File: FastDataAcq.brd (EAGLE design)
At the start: 114.3 x 62.7 mm, 215 parts, among them IC1 LT1963AEQ, IC2 FT230XQ, IC3 ADCMP553BRMZ, J1 MICRO-FIT_3.0_2POS_RA_SMD, J2 USB_MICROAB_SMT, X1 87832-14, X2 SMA-142-0701-801/806, X3 SMA-142-0701-801/806, Y1 SI530-500, Y2 100MHz, Y3 DNP

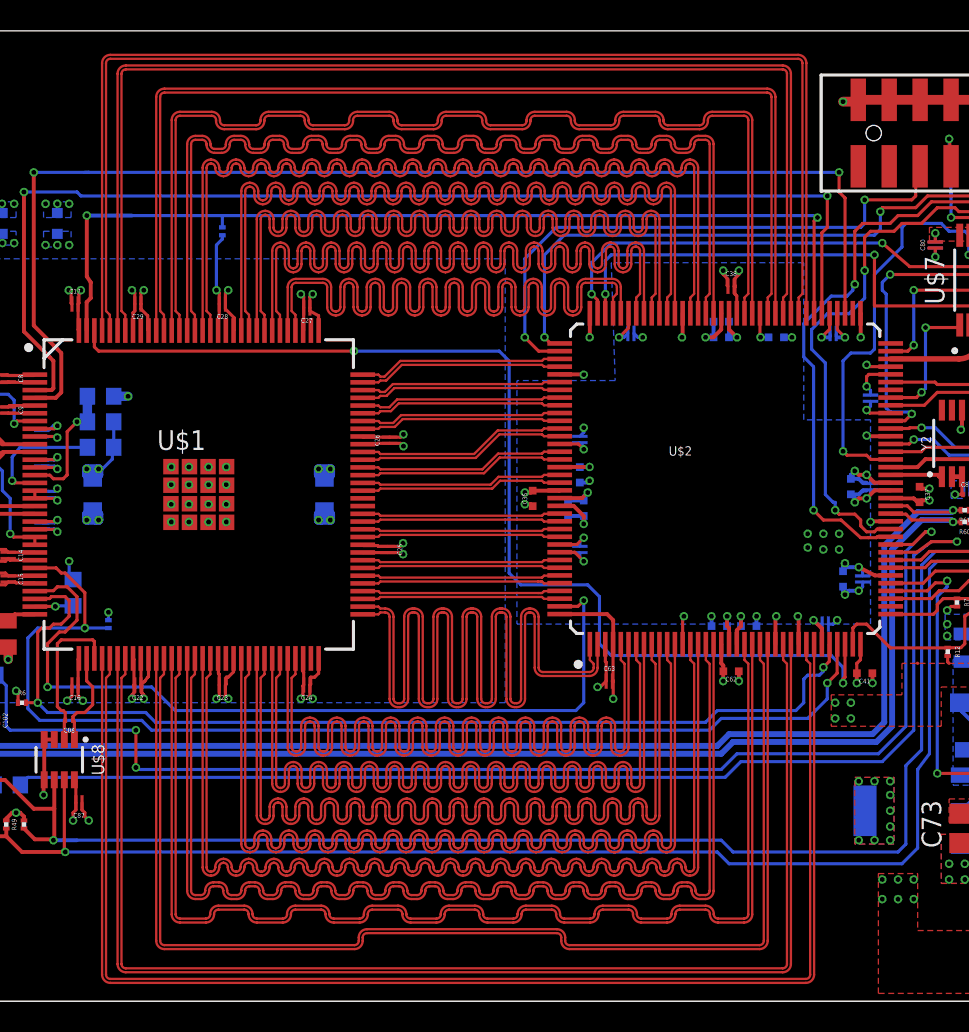
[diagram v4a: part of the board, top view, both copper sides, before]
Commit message: LVDS Top Changed
Changed LVDS data lines to 5mil width and spacing. Bend separation is
25mil.  Only the top data lines are finished - still need to do the
bottom and sides.
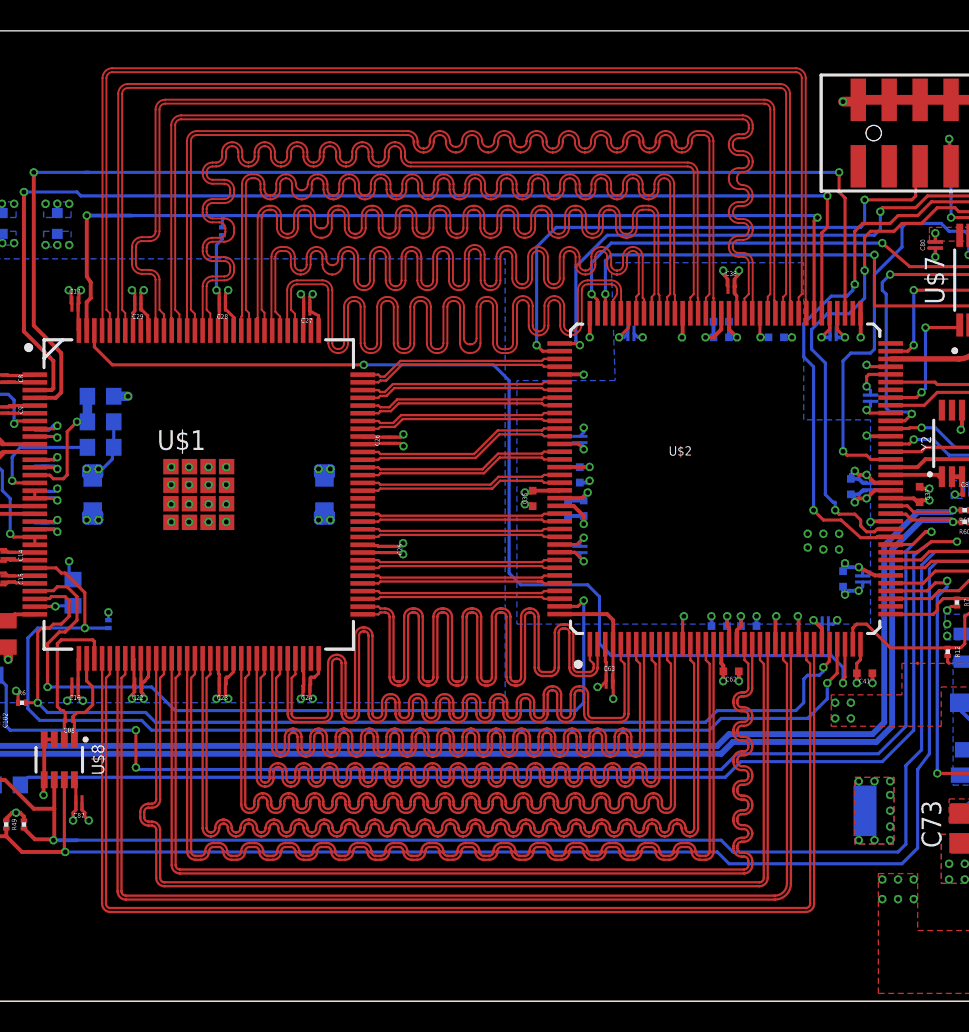
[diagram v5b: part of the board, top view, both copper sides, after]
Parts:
- C7, C75: value NA -> DNP
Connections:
- net DI0+ renamed DI0_P
- net DI0- renamed DI0_N
- net DI1+ renamed DI1_P
- net DI1- renamed DI1_N
- net DID0+ renamed DID0_P
- net DID0- renamed DID0_N
- net DID1+ renamed DID1_P
- net DID1- renamed DID1_N
- net DID2+ renamed DID2_P
- net DID2- renamed DID2_N
- net DID3+ renamed DID3_P
- net DID3- renamed DID3_N
- net DID4+ renamed DID4_P
- net DID4- renamed DID4_N
- net DID5+ renamed DID5_P
- net DID5- renamed DID5_N
- net DID6+ renamed DID6_P
- net DID6- renamed DID6_N
- net DID7+ renamed DID7_P
- net DID7- renamed DID7_N
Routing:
- net DQD1-: track 83.9 -> 74.2 mm
- net DQD1+: track 84.4 -> 74.7 mm
- net DI1_N: track 58.5 -> 67.9 mm
- net DQD0-: track 87.8 -> 78.6 mm
- net DQD0+: track 88.3 -> 79.1 mm
- net DQD6-: track 74.2 -> 65.0 mm
- net DQD6+: track 74.7 -> 65.6 mm
- net DQ2-: track 76.9 -> 68.1 mm
- net DQ2+: track 77.1 -> 68.3 mm
- net DI1_P: track 59.0 -> 67.8 mm
- net DQD7-: track 74.4 -> 65.8 mm
- net DQD7+: track 75.0 -> 66.3 mm
- net DQ0+: track 75.2 -> 67.1 mm
- net DQ0-: track 74.7 -> 66.6 mm
- net DQD2-: track 78.0 -> 69.9 mm
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
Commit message: Partially done with LVDS bottom half.
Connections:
- net DQ0+ renamed DQ0_P
- net DQ0- renamed DQ0_N
- net DQ1+ renamed DQ1_P
- net DQ1- renamed DQ1_N
- net DQ2+ renamed DQ2_P
- net DQ2- renamed DQ2_N
- net DQD0+ renamed DQD0_P
- net DQD0- renamed DQD0_N
- net DQD1+ renamed DQD1_P
- net DQD1- renamed DQD1_N
- net DQD2+ renamed DQD2_P
- net DQD2- renamed DQD2_N
- net DQD3+ renamed DQD3_P
- net DQD3- renamed DQD3_N
- net DQD4+ renamed DQD4_P
- net DQD4- renamed DQD4_N
- net DQD5+ renamed DQD5_P
- net DQD5- renamed DQD5_N
- net DQD6+ renamed DQD6_P
- net DQD6- renamed DQD6_N
- net DQD7+ renamed DQD7_P
- net DQD7- renamed DQD7_N
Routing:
- net DQD1_P: track 74.7 -> 81.4 mm
- net DQD1_N: track 74.2 -> 80.8 mm
- net DQD0_P: track 79.1 -> 85.7 mm
- net DQD0_N: track 78.6 -> 85.1 mm
- net DQD6_P: track 65.6 -> 71.6 mm
- net DQD7_N: track 65.8 -> 71.8 mm
- net DQD6_N: track 65.0 -> 71.0 mm
- net DQD7_P: track 66.3 -> 72.2 mm
- net DQ1_N: track 67.1 -> 72.4 mm
- net DQD2_P: track 70.4 -> 75.6 mm
- net DQ2_N: track 68.1 -> 73.2 mm
- net DQ0_N: track 66.6 -> 71.6 mm
- net DQD2_N: track 69.9 -> 74.9 mm
- net DQ2_P: track 68.3 -> 73.2 mm
- net DQ1_P: track 67.6 -> 72.4 mm
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
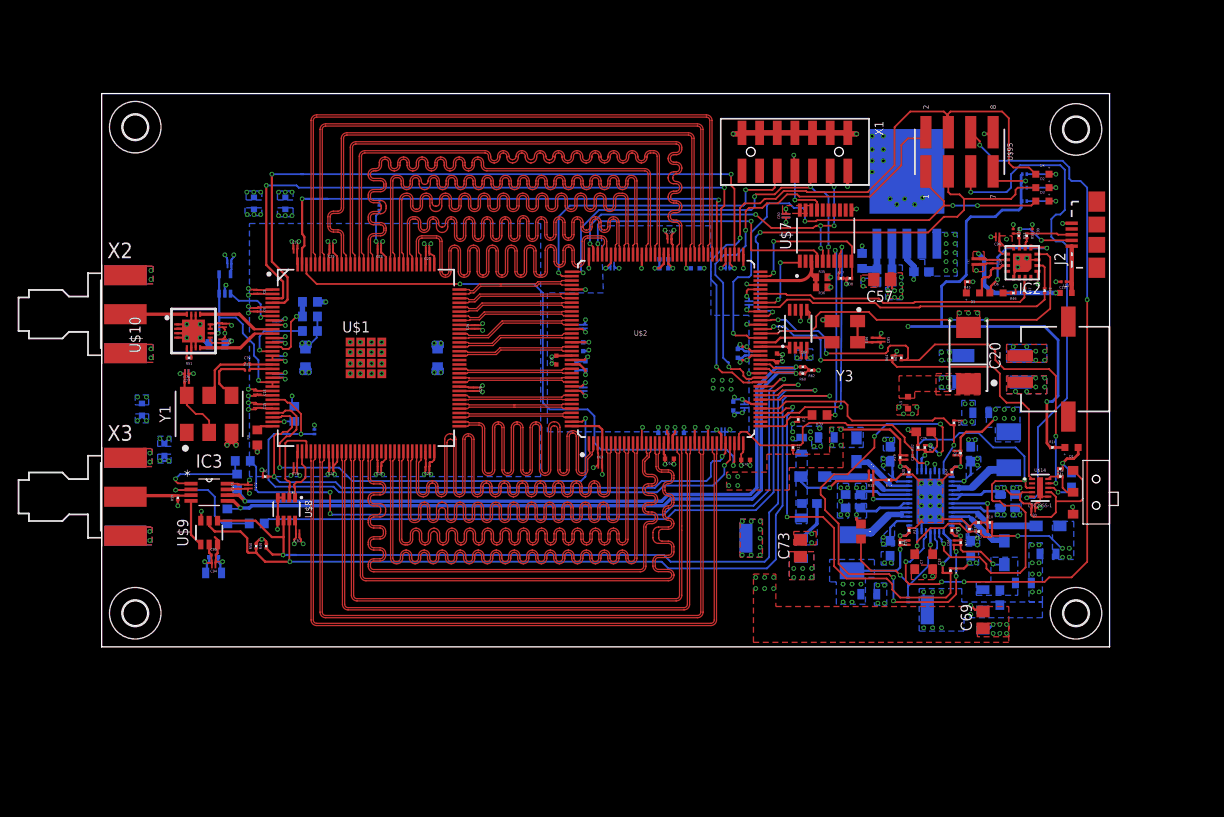
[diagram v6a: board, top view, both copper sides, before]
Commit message: Finished LVDS layout.
Making additional final changes. Still need to add test points.
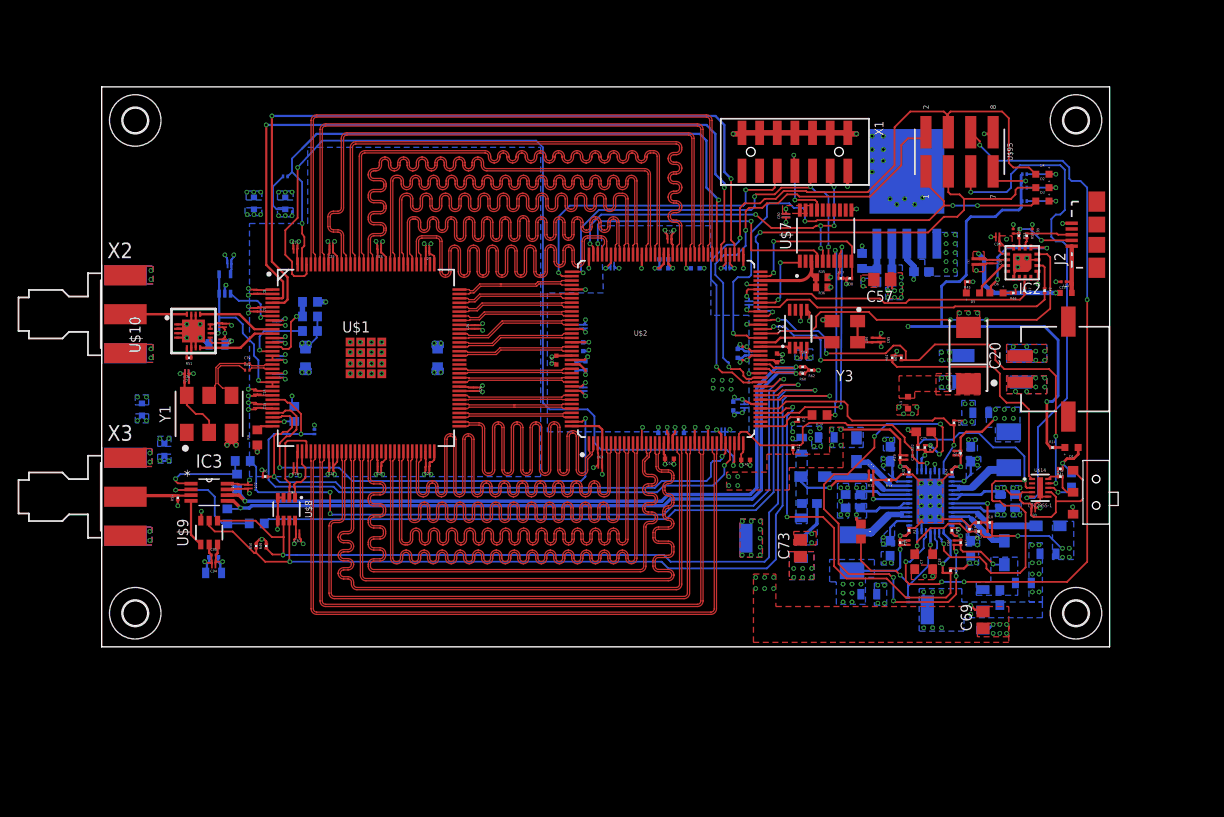
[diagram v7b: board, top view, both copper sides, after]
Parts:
- moved R1 11.2 mm to (20.8, 70.6), turned to 0 degrees
- moved H2 1.02 mm to (110.5, 77.0)
- moved H4 0.76 mm to (3.81, 77.0)
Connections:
- net ADC_CLK+ renamed ADC_CLK_P
- net ADC_CLK- renamed ADC_CLK_N
- net CLK500+ renamed CLK500_P
- net CLK500- renamed CLK500_N
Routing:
- net ADC_CALRUN: track 70.7 -> 103.8 mm
- net ADC_CALDLY/DES/!SCS: track 62.3 -> 75.6 mm
- net ADC_OUTV/SCLK: track 74.5 -> 87.2 mm
- net ADC_OUTEDGE/DDR/SDATA: track 78.4 -> 90.3 mm
- net DQD3_P: track 71.7 -> 74.6 mm
- net DQD3_N: track 71.0 -> 73.9 mm
- net DQD0_P: track 85.7 -> 83.1 mm
- net DQD1_P: track 81.4 -> 78.8 mm
- net DQD1_N: track 80.8 -> 78.2 mm
- net DQD0_N: track 85.1 -> 82.6 mm
- net 1V9D: track 29.2 -> 31.3 mm
- net GND: track 234.0 -> 233.0 mm
- net FPGA_SCL: track 105.2 -> 104.3 mm
- net DQD4_P: track 73.4 -> 74.2 mm
- net PWR_KILL: track 55.4 -> 54.6 mm
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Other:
- board size 114.3 x 62.7 mm -> 114.3 x 63.5 mm
- board text added: "Manufacturer Notes: 1. All copper thickness is 1oz 2. LVDS lines are 5mil width with 5mil spacing and should have a 100 Ohms+/- 10% differential impedance. 3. Layer height is betwen 7 and 8 mils."

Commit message: Parts finalized. Layout near done.
Still a few things on the to do list, but most tracks are final. Still
need test points and to go over all text that's getting printed.
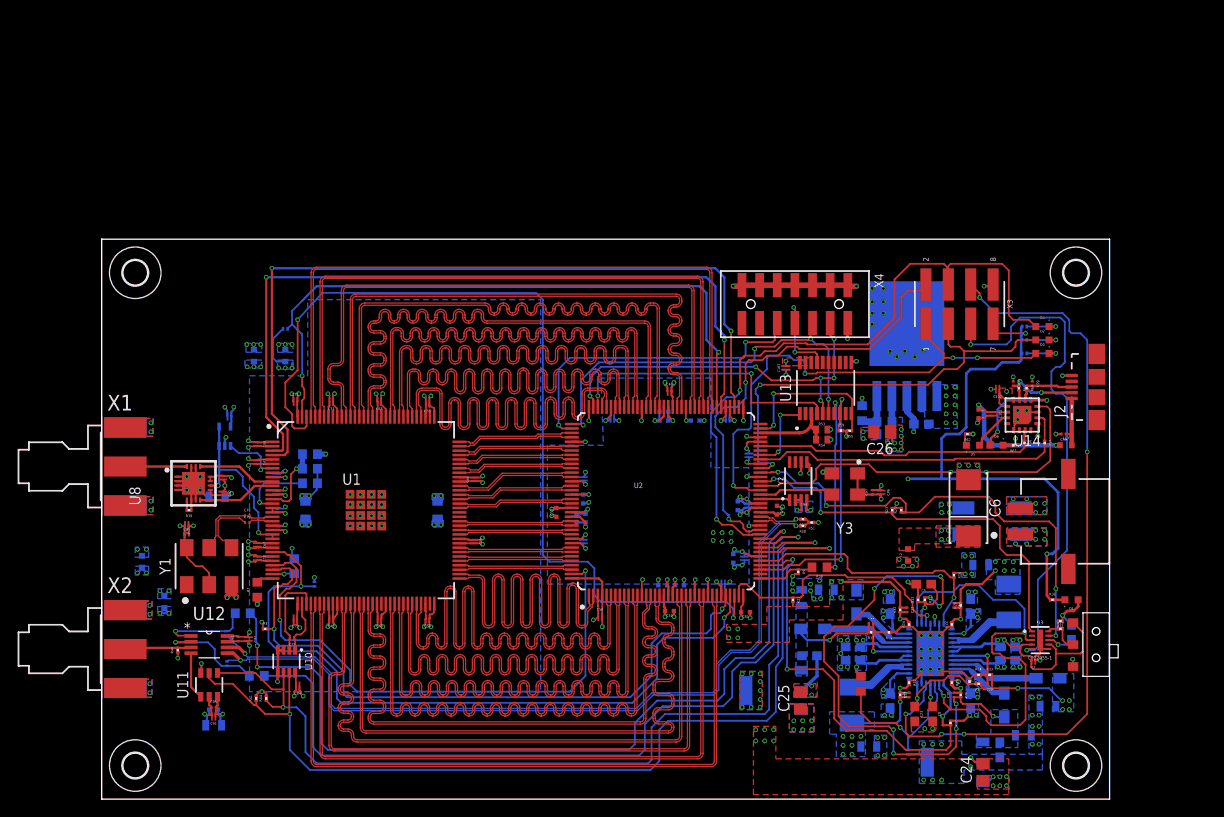
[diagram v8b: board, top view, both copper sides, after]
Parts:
- removed IC1: LT1963AEQ, linear-technology:Q5-DD
- removed IC2: FT230XQ, ftdichip:QFN16
- removed IC3: ADCMP553BRMZ, Schuyler:SOP65P490X110-8N
- removed R64: 523K, rcl:R0201
- removed U$1: ADC08D500, Schuyler:128HLQFP
- removed U$10: LMH6555, Schuyler:16WQFN
- removed U$11: LMV321SC-70, Schuyler:SC-70
- removed U$14: LTC2955-1, Schuyler:10-DFN
- removed U$2: XC6SLX9-3TQG144C, Schuyler:TQG144
- removed U$4: LTC3374QFN, Schuyler:38-QFN_(5X7)
- removed U$5: LT1963AEST-2.5, Schuyler:SOT223
- removed U$6: LT1963AEST-3.3, Schuyler:SOT223
- removed U$7: XCFXXS04, Schuyler:TSSOP20_XILINX
- removed U$8: TMP421, Schuyler:SOT23-8
- removed U$9: DAC101C081, Schuyler:SOT23-6
- removed U$95: HEADER_0.1"_8P_2R_SMT, Schuyler:HEADER_8P_2R_SMT
- added R58: 0, rcl:R0603
- added U1: ADC08D500, Schuyler:128HLQFP
- added U10: TMP421, Schuyler:SOT23-8
- added U11: DAC101C081, Schuyler:SOT23-6
- added U12: ADCMP553BRMZ, Schuyler:SOP65P490X110-8N
- added U13: XCFXXS04, Schuyler:TSSOP20_XILINX
- added U14: FT230XQ, ftdichip:QFN16
- added U2: XC6SLX9-3TQG144C, Schuyler:TQG144
- added U3: LTC2955-1, Schuyler:10-DFN
- added U4: LT1963AEST-2.5, Schuyler:SOT223
- added U5: LT1963AEST-3.3, Schuyler:SOT223
- added U6: LT1963AEQ, linear-technology:Q5-DD
- added U7: LTC3374QFN, Schuyler:38-QFN_(5X7)
- added U8: LMH6555, Schuyler:16WQFN
- added U9: LMV321SC-70, Schuyler:SC-70
- added X4: 87832-14, con-molex:87832-14
- C10, C11, C14, C27, C28, C29: value .1uF -> 10pF; device Schuyler:0204REVERSE -> rcl:C0201
- C101, C103, C84, C86: value 10nF -> .1uF; device rcl:C0201 -> Schuyler:0204REVERSE
- C102, C81: value 1uF -> .1uF
- C104, C87, C90: value .1uF -> 1uF
- C105: value DNP -> 4.7uF; device rcl:C0603 -> Schuyler:0402_C
- C12, C13, C15, C30, C83: value .1uF -> 33uF; device Schuyler:0204REVERSE -> SparkFun-Passives:0805
- C16, C17, C22, C8: value .1uF -> 10uF; device Schuyler:0204REVERSE -> rcl:C0603
- C19, C3: value 33uF -> 10uF; device SparkFun-Passives:0805 -> rcl:C0603
- C2: value 10pF -> 10uF; device rcl:C0201 -> rcl:C0603
- C20: value 100uF -> 10uF; device Schuyler:2917_MURATA_CAP -> rcl:C0603
- C23, C9: value .1uF -> DNP; device Schuyler:0204REVERSE -> rcl:C0603
- C24, C25, C26: value .1uF -> 22uF 150mOhm ESR; device Schuyler:0204REVERSE -> rcl:C0805
- C32: value 10uF -> 33uF; device rcl:C0603 -> SparkFun-Passives:0805
- C33, C66: value 10pF -> 4.7uF; device rcl:C0201 -> Schuyler:0402_C
- C34, C74: value 33uF -> 4.7uF; device SparkFun-Passives:0805 -> Schuyler:0402_C
- C37, C42, C43, C62: value 4.7uF -> 0.47uF; device Schuyler:0402_C -> Schuyler:0204REVERSE
- C39, C40: value 4.7uF -> 33uF; device Schuyler:0402_C -> SparkFun-Passives:0805
- C44, C45, C47, C50, C59: value 4.7uF -> .1uF; device Schuyler:0402_C -> Schuyler:0204REVERSE
- C48, C49, C60, C64: value 0.47uF -> .1uF
- C5: value 10pF -> DNP; device rcl:C0201 -> rcl:C0603
- C51, C52, C61: value 0.47uF -> 4.7uF; device Schuyler:0204REVERSE -> Schuyler:0402_C
- C53, C72: value 10uF -> 4.7uF; device rcl:C0603 -> Schuyler:0402_C
- C54, C71: value 10pF -> .1uF; device rcl:C0201 -> Schuyler:0204REVERSE
- C55, C67, C91: value 33uF -> .1uF; device SparkFun-Passives:0805 -> Schuyler:0204REVERSE
- C56, C58: value 10uF -> 0.47uF; device rcl:C0603 -> Schuyler:0204REVERSE
- C57, C69: value 22uF 150mOhm ESR -> 4.7uF; device rcl:C0805 -> Schuyler:0402_C
- C6: value 33uF -> 100uF; device SparkFun-Passives:0805 -> Schuyler:2917_MURATA_CAP
- C65, C68, C70: value 10uF -> .1uF; device rcl:C0603 -> Schuyler:0204REVERSE
- C7, C75: value DNP -> .1uF; device rcl:C0603 -> Schuyler:0204REVERSE
- C73: value 22uF 150mOhm ESR -> .1uF; device rcl:C0805 -> Schuyler:0204REVERSE
- C76: value 10nF -> 0.47uF; device rcl:C0201 -> Schuyler:0204REVERSE
- C77: value .1uF -> 100pF; device Schuyler:0204REVERSE -> rcl:C0201
- C78: value 1uF -> 4.7nF; device Schuyler:0204REVERSE -> rcl:C0201
- C82: value 4.7nF -> .1uF; device rcl:C0201 -> Schuyler:0204REVERSE
- C85, C94, C97: value .1uF -> 10nF; device Schuyler:0204REVERSE -> rcl:C0201
- C88: value 100pF -> 33uF; device rcl:C0201 -> SparkFun-Passives:0805
- C89: value .1uF -> 4.7uF; device Schuyler:0204REVERSE -> Schuyler:0402_C
- C92: value 4.7uF -> .1uF; device Schuyler:0306REVERSE -> Schuyler:0204REVERSE
- C93: value 4.7uF -> 10nF; device Schuyler:0402_C -> rcl:C0201
- C98: value 33uF -> 10nF; device SparkFun-Passives:0805 -> rcl:C0201
- L1: value 2.2uH -> CHOKE_CM_ACM7060-301; device Schuyler:3.0X3.6_VISHAY -> Schuyler:ACM7060_CHOKE
- L10, L9: value 2.2uH -> 26; device Schuyler:3.0X3.6_VISHAY -> Schuyler:MURATA_BLM18
- L2: value CHOKE_CM_ACM7060-301 -> 26; device Schuyler:ACM7060_CHOKE -> Schuyler:MURATA_BLM18
- L3: device Schuyler:5.18X5.49_VISHAY -> Schuyler:3.0X3.6_VISHAY
- L4, L6: value 26 -> 2.2uH; device Schuyler:MURATA_BLM18 -> Schuyler:3.0X3.6_VISHAY
- L5: value 26 -> 2.2uH; device Schuyler:MURATA_BLM18 -> Schuyler:5.18X5.49_VISHAY
- R1, R6: value 10k -> DNP; device rcl:R0201 -> rcl:R0603
- R10, R16: value 210K -> 523K
- R11: value 422K -> 649K
- R12: value 10k -> 150K
- R13, R17: value 270k -> 523K
- R14: value 330 -> 523K
- R15: value 845k -> 113k
- R18, R28: value 523K -> 210K
- R19: value 806K -> 150K
- R20: value 649K -> 523K
- R21: value 523K -> 10k
- R22: value 1.15k 1% -> 280K; device rcl:R0603 -> rcl:R0201
- R24: value 280K -> 523K
- R25: value 100 -> 523K; device rcl:R0603 -> rcl:R0201
- R26: value 2k 1% -> DNP
- R27: value 523K -> 270k
- R29: value 210K -> 1.15k 1%; device rcl:R0201 -> rcl:R0603
- R3, R8: value DNP -> 10k; device rcl:R0603 -> rcl:R0201
- R30: value 649K -> 2k 1%; device rcl:R0201 -> rcl:R0603
- R31: value 523K -> 100; device rcl:R0201 -> rcl:R0603
- R32: value 150K -> 806K
- R33: value 150K -> 210K
- R34: value 523K -> 649K
- R35: value 100 0.1% -> 845k; device rcl:R0402 -> rcl:R0201
- R36: value 100 0.1% -> 422K; device rcl:R0402 -> rcl:R0201
- R37: value 4.7k -> 270k
- R39: value 0 -> 50; device rcl:R0603 -> rcl:R0201
- R40: value DNP -> 50; device rcl:R0603 -> rcl:R0201
- R41: value 113k -> 10k
- R42: value 330 -> 26.1k; device rcl:R0201 -> rcl:R0603
- R43, R44, R47: value 330 -> 10k
- R46: value 330 -> 16k; device rcl:R0201 -> rcl:R0603
- R49: value 10k -> 330
- R50: value 10k -> 50
- R52: value 27 -> 50
- R53: value 27 -> 100 0.1%; device rcl:R0201 -> rcl:R0402
- R54: value 26.1k -> 100 0.1%; device rcl:R0603 -> rcl:R0402
- R55: value 16k -> 330; device rcl:R0603 -> rcl:R0201
- R56, R57: value 10k -> 330; device rcl:R0603 -> rcl:R0201
- R59: value 50 -> 4.7k
- R60, R61: value 50 -> 27
- R62: value 50 -> 330
- R63: value 523K -> 330
- R7: value 4.7k -> 3.3k 0.1%; device rcl:R0201 -> rcl:R0603
- R9: value 3.3k 0.1% -> 4.7k; device rcl:R0603 -> rcl:R0201
- X1: value 87832-14 -> SMA-142-0701-801/806; device con-molex:87832-14 -> con-coax:J502-ND-142-0701-801/806
- X3: value SMA-142-0701-801/806 -> HEADER_0.1"_8P_2R_SMT; device con-coax:J502-ND-142-0701-801/806 -> Schuyler:HEADER_8P_2R_SMT
- moved R44 104.5 mm to (18.7, 11.4), flipped to the top, turned to 90 degrees
- moved R43 103.0 mm to (14.1, 18.8), turned to 270 degrees
- moved R42 100.9 mm to (16.0, 21.1), turned to 0 degrees
- moved R47 99.8 mm to (14.2, 15.4), flipped to the bottom, turned to 90 degrees
- moved X3 99.7 mm to (97.3, 56.1)
- moved C9 99.3 mm to (110.0, 18.9), flipped to the bottom
- moved C98 97.7 mm to (109.1, 41.4), flipped to the top
- moved R46 96.1 mm to (17.6, 14.0), flipped to the bottom, turned to 0 degrees
- moved C12 94.9 mm to (104.5, 7.24), turned to 180 degrees
- moved R41 94.8 mm to (17.5, 11.4), turned to 90 degrees
- moved R57 91.7 mm to (106.9, 40.4), flipped to the top
- moved R56 90.8 mm to (104.6, 40.4), flipped to the top, turned to 270 degrees
- moved C8 90.3 mm to (94.2, 9.65), turned to 270 degrees
- moved R49 89.5 mm to (104.6, 53.6), flipped to the bottom, turned to 180 degrees
- moved L9 88.0 mm to (17.3, 50.3), turned to 90 degrees
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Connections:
- removed net FPGA_TRIG+: IC3.6, R57.2, R61.2, U$2.P$51
- removed net FPGA_TRIG-: IC3.5, R56.2, R60.2, U$2.P$50
- new net FPGA_TRIG_N: R47.2, R50.2, U12.5, U2.P$50
- new net FPGA_TRIG_P: R43.2, R52.2, U12.6, U2.P$51
- net !PB: now also U3.P$5, X3.P$5; no longer U$14.P$5, U$95.P$5
- net !RXLED: now also U14.11; no longer IC2.11
- net !TXLED: now also U14.5; no longer IC2.5
- net 1V2: now also C28.1, C31.1, C33.P$1, C41.P$1, C46.P$1, L7.P$2, R27.1, R33.2, U2.P$128, U2.P$19, U2.P$28, U2.P$52, U2.P$89; no longer C2.1, C3.1, C35.P$1, C37.P$1, C38.P$1, L1.P$2, R10.2, R13.1, U$2.P$128, U$2.P$19, U$2.P$28, U$2.P$52, U$2.P$89
- net 1V8: now also C27.1, C30.1, C34.P$1, C38.P$1, C42.P$1, C56.P$1, C58.P$1, L6.P$2, R21.2, R32.2, U2.P$103, U2.P$122, U2.P$125, U2.P$135, U2.P$144, U2.P$18, U2.P$31, U2.P$4, U2.P$76, U2.P$86; no longer C33.1, C34.1, C47.P$1, C48.P$1, C49.P$1, C50.P$1, C64.P$1, L7.P$2, R12.2, R19.2, U$2.P$103, U$2.P$122, U$2.P$125, U$2.P$135, U$2.P$144, U$2.P$18, U$2.P$31, U$2.P$4, U$2.P$76, U$2.P$86
- net 1V9: now also C26.1, L10.P$1, L9.P$1, R29.2, R31.2, U6.4; no longer C57.1, IC1.4, L4.P$1, L6.P$1, R22.2, R25.2
- net 1V9A: now also C39.1, C44.P$1, C47.P$2, C49.P$2, C54.P$1, C59.P$1, C64.P$2, C67.P$1, C70.P$1, C73.P$2, C75.P$1, L9.P$2, R3.1, R6.2, U1.P$128, U1.P$13, U1.P$16, U1.P$17, U1.P$2, U1.P$20, U1.P$25, U1.P$28, U1.P$33, U1.P$5, U1.P$8; no longer C10.P$2, C11.P$1, C12.P$1, C13.P$2, C14.P$1, C15.P$1, C16.P$2, C17.P$1, C19.1, C8.P$1, C9.P$2, L4.P$2, R6.1, R8.2, U$1.P$128, U$1.P$13, U$1.P$16, U$1.P$17, U$1.P$2, U$1.P$20, U$1.P$25, U$1.P$28, U$1.P$33, U$1.P$5, U$1.P$8
- net 1V9D: now also C40.1, C45.P$1, C48.P$1, C50.P$1, C55.P$1, C60.P$1, C65.P$1, C68.P$1, C71.P$1, L10.P$2, R8.2, U1.P$110, U1.P$121, U1.P$40, U1.P$51, U1.P$62, U1.P$73, U1.P$88, U1.P$99; no longer C22.P$1, C23.P$1, C24.P$1, C25.P$1, C26.P$1, C27.P$1, C28.P$1, C29.P$1, C31.1, L6.P$2, R2.2, U$1.P$110, U$1.P$121, U$1.P$40, U$1.P$51, U$1.P$62, U$1.P$73, U$1.P$88, U$1.P$99
- net 2V3_1V9PRE: now also C14.1, C15.1, C19.1, L5.P$2, R20.2, U6.1, U6.2; no longer C54.1, C55.1, C56.1, IC1.1, IC1.2, L8.P$2, R21.2
- net 2V5: now also C24.1, L12.P$2, U4.3; no longer C69.1, L11.P$2, U$5.3
- net 2V5A: now also C85.1, C86.P$1, C87.P$1, L12.P$1; no longer C76.1, C77.P$1, C78.P$1, L11.P$1
- net 2V8_2V5PRE: now also C10.1, C12.1, C16.1, L3.P$2, R11.1, R16.2, U4.1; no longer C66.1, C67.1, C68.1, L9.P$2, R27.2, R30.1, U$5.1
- net 3V3: now also C104.P$1, C29.1, C32.1, C35.P$1, C37.P$1, C53.P$1, C57.P$1, C66.P$1, C69.P$1, C72.P$1, C74.P$1, C76.P$1, C84.P$1, C88.1, C89.P$1, C90.P$1, C91.P$1, C92.P$1, C93.1, C94.1, C96.P$1, C97.1, L8.P$2, R23.2, R25.2, R38.1, R41.2, R44.2, R45.1, R48.1, R49.1, R53.2, R55.2, R59.2, R9.2, U10.P$8, U11.P$2, U12.7, U13.P$18, U13.P$19, U13.P$20, U2.P$129, U2.P$20, U2.P$36, U2.P$42, U2.P$53, U2.P$63, U2.P$69, U2.P$90, X3.P$7, X4.2; no longer C103.1, C39.P$1, C40.P$1, C41.P$1, C42.P$1, C44.P$1, C45.P$1, C46.P$1, C5.1, C59.P$1, C6.1, C60.P$1, C80.P$1, C81.P$1, C83.P$1, C84.1, C85.P$1, C86.1, C87.P$1, C93.P$1, C94.P$1, C98.1, IC3.7, L3.P$2, R14.1, R15.2, R37.2, R38.2, R42.1, R43.1, R44.1, R49.2, R50.2, R63.2, R64.2, R7.2, U$2.P$129, U$2.P$20, U$2.P$36, U$2.P$42, U$2.P$53, U$2.P$63, U$2.P$69, U$2.P$90, U$7.P$18, U$7.P$19, U$7.P$20, U$8.P$8, U$9.P$2, U$95.P$7, X1.2
- net 3V3A: now also C25.1, L11.P$2, U5.3; no longer C73.1, L12.P$2, U$6.3
- net 3V3OUT: now also C101.P$2, R62.1, R63.1, U14.1, U14.8, U14.9; no longer C96.P$2, IC2.1, IC2.8, IC2.9, R45.1, R46.1
- net 3V3S: now also C80.P$1, C81.P$1, C82.P$1, C83.1, L11.P$1, U8.P$11, U8.P$12, U8.P$9, U9.P$5; no longer C104.P$1, C89.P$1, C90.P$1, C91.1, L12.P$1, U$10.P$11, U$10.P$12, U$10.P$9, U$11.P$5
- net 3V6_PRE3V3: now also C11.1, C13.1, C17.1, L4.P$2, R17.2, U5.1; no longer C71.1, C72.1, C74.1, L10.P$2, R31.2, U$6.1
- net 5VUSB: now also C103.P$2, C105.P$2, U14.10; no longer C92.P$1, C97.P$2, IC2.10
- net 5VUSB_CON: now also C98.1; no longer C101.1
- net ADC_CAL: now also R3.2, U1.P$30, U2.P$32; no longer R6.2, U$1.P$30, U$2.P$32
- net ADC_CALDLY/DES/!SCS: now also R8.1, U1.P$127, U2.P$79; no longer R1.1, U$1.P$127, U$2.P$79
- net ADC_CALRUN: now also U1.P$126, U2.P$34; no longer U$1.P$126, U$2.P$34
- net ADC_CLK_N: now also C79.2, U1.P$19; no longer C82.2, U$1.P$19
- net ADC_CLK_P: now also C78.2, U1.P$18; no longer C79.2, U$1.P$18
- net ADC_DCLKRST: now also U1.P$15; no longer U$1.P$15
- net ADC_DCLK_N: now also U1.P$81, U2.P$127; no longer U$1.P$81, U$2.P$127
- net ADC_DCLK_P: now also U1.P$82, U2.P$126; no longer U$1.P$82, U$2.P$126
- net ADC_FSR/ECE: now also R1.1, R2.2, U1.P$14; no longer R2.1, R3.2, U$1.P$14
- net ADC_OUTEDGE/DDR/SDATA: now also U1.P$4, U2.P$75; no longer U$1.P$4, U$2.P$75
- net ADC_OUTV/SCLK: now also U1.P$3, U2.P$78; no longer U$1.P$3, U$2.P$78
- net ADC_PD: now also U1.P$26, U2.P$33; no longer U$1.P$26, U$2.P$33
- net ADC_PDQ: now also U1.P$29, U2.P$143; no longer U$1.P$29, U$2.P$143
- net ADC_PWR_EN: now also R14.2, U2.P$41, U7.P$19; no longer R23.2, U$2.P$41, U$4.P$19
- net ADC_REXT: now also R7.2, U1.P$32; no longer R9.2, U$1.P$32
- net ADC_TDIODE+: now also C77.1, U1.P$34, U10.P$1; no longer C88.1, U$1.P$34, U$8.P$1
- net ADC_TDIODE-: now also C77.2, U1.P$35, U10.P$2; no longer C88.2, U$1.P$35, U$8.P$2
- net ADC_VBG: now also R6.1, U1.P$31; no longer R8.1, U$1.P$31
- net ADC_VCMO: now also U1.P$7, U9.P$1; no longer U$1.P$7, U$11.P$1
- net ADC_VCMO_BUFFER: now also U1.P$22, U1.P$23, U8.P$10, U9.P$3, U9.P$4; no longer U$1.P$22, U$1.P$23, U$10.P$10, U$11.P$3, U$11.P$4
- net ADC_VINI+: now also U1.P$11, U8.P$8; no longer U$1.P$11, U$10.P$8
- net ADC_VINI-: now also U1.P$10, U8.P$13; no longer U$1.P$10, U$10.P$13
- net ANALOG_PWR_EN: now also R10.2, U2.P$40, U7.P$32; no longer R28.2, U$2.P$40, U$4.P$32
- net CLK500_N: now also C78.1; no longer C79.1
- net CLK500_P: now also C79.1; no longer C82.1
- net DI0_N: now also U1.P$102, U2.P$102; no longer U$1.P$102, U$2.P$102
- net DI0_P: now also U1.P$103, U2.P$101; no longer U$1.P$103, U$2.P$101
- net DI1_N: now also U1.P$100, U2.P$105; no longer U$1.P$100, U$2.P$105
- net DI1_P: now also U1.P$101, U2.P$104; no longer U$1.P$101, U$2.P$104
- net DI2_N: now also U1.P$95, U2.P$112; no longer U$1.P$95, U$2.P$112
- net DI2_P: now also U1.P$96, U2.P$111; no longer U$1.P$96, U$2.P$111
- net DI3_N: now also U1.P$93, U2.P$115; no longer U$1.P$93, U$2.P$115
- net DI3_P: now also U1.P$94, U2.P$114; no longer U$1.P$94, U$2.P$114
- net DI4_N: now also U1.P$91, U2.P$117; no longer U$1.P$91, U$2.P$117
- net DI4_P: now also U1.P$92, U2.P$116; no longer U$1.P$92, U$2.P$116
- net DI5_N: now also U1.P$89, U2.P$119; no longer U$1.P$89, U$2.P$119
- net DI5_P: now also U1.P$90, U2.P$118; no longer U$1.P$90, U$2.P$118
- net DI6_N: now also U1.P$85, U2.P$121; no longer U$1.P$85, U$2.P$121
- net DI6_P: now also U1.P$86, U2.P$120; no longer U$1.P$86, U$2.P$120
- net DI7_N: now also U1.P$83, U2.P$124; no longer U$1.P$83, U$2.P$124
- net DI7_P: now also U1.P$84, U2.P$123; no longer U$1.P$84, U$2.P$123
- net DID0_N: now also U1.P$124, U2.P$81; no longer U$1.P$124, U$2.P$81
- net DID0_P: now also U1.P$125, U2.P$80; no longer U$1.P$125, U$2.P$80
- net DID1_N: now also U1.P$122, U2.P$83; no longer U$1.P$122, U$2.P$83
- net DID1_P: now also U1.P$123, U2.P$82; no longer U$1.P$123, U$2.P$82
- net DID2_N: now also U1.P$117, U2.P$85; no longer U$1.P$117, U$2.P$85
- net DID2_P: now also U1.P$118, U2.P$84; no longer U$1.P$118, U$2.P$84
- net DID3_N: now also U1.P$115, U2.P$88; no longer U$1.P$115, U$2.P$88
- net DID3_P: now also U1.P$116, U2.P$87; no longer U$1.P$116, U$2.P$87
- net DID4_N: now also U1.P$113, U2.P$93; no longer U$1.P$113, U$2.P$93
- net DID4_P: now also U1.P$114, U2.P$92; no longer U$1.P$114, U$2.P$92
- net DID5_N: now also U1.P$111, U2.P$95; no longer U$1.P$111, U$2.P$95
- net DID5_P: now also U1.P$112, U2.P$94; no longer U$1.P$112, U$2.P$94
- net DID6_N: now also U1.P$106, U2.P$98; no longer U$1.P$106, U$2.P$98
- net DID6_P: now also U1.P$107, U2.P$97; no longer U$1.P$107, U$2.P$97
- net DID7_N: now also U1.P$104, U2.P$100; no longer U$1.P$104, U$2.P$100
- net DID7_P: now also U1.P$105, U2.P$99; no longer U$1.P$105, U$2.P$99
- net DQ0_N: now also U1.P$59, U2.P$7; no longer U$1.P$59, U$2.P$7
- net DQ0_P: now also U1.P$58, U2.P$8; no longer U$1.P$58, U$2.P$8
- net DQ1_N: now also U1.P$61, U2.P$5; no longer U$1.P$61, U$2.P$5
- net DQ1_P: now also U1.P$60, U2.P$6; no longer U$1.P$60, U$2.P$6
- net DQ2_N: now also U1.P$66, U2.P$1; no longer U$1.P$66, U$2.P$1
- net DQ2_P: now also U1.P$65, U2.P$2; no longer U$1.P$65, U$2.P$2
- net DQ3_N: now also U1.P$67, U2.P$142; no longer U$1.P$67, U$2.P$142
- net DQ3_P: now also U1.P$68, U2.P$141; no longer U$1.P$68, U$2.P$141
- net DQ4_N: now also U1.P$69, U2.P$140; no longer U$1.P$69, U$2.P$140
- net DQ4_P: now also U1.P$70, U2.P$139; no longer U$1.P$70, U$2.P$139
- net DQ5_N: now also U1.P$71, U2.P$138; no longer U$1.P$71, U$2.P$138
- net DQ5_P: now also U1.P$72, U2.P$137; no longer U$1.P$72, U$2.P$137
- net DQ6_N: now also U1.P$75, U2.P$134; no longer U$1.P$75, U$2.P$134
- net DQ6_P: now also U1.P$76, U2.P$133; no longer U$1.P$76, U$2.P$133
- net DQ7_N: now also U1.P$77, U2.P$132; no longer U$1.P$77, U$2.P$132
- net DQ7_P: now also U1.P$78, U2.P$131; no longer U$1.P$78, U$2.P$131
- net DQD0_N: now also U1.P$37, U2.P$29; no longer U$1.P$37, U$2.P$29
- net DQD0_P: now also U1.P$36, U2.P$30; no longer U$1.P$36, U$2.P$30
- net DQD1_N: now also U1.P$39, U2.P$26; no longer U$1.P$39, U$2.P$26
- net DQD1_P: now also U1.P$38, U2.P$27; no longer U$1.P$38, U$2.P$27
- net DQD2_N: now also U1.P$44, U2.P$23; no longer U$1.P$44, U$2.P$23
- net DQD2_P: now also U1.P$43, U2.P$24; no longer U$1.P$43, U$2.P$24
- net DQD3_N: now also U1.P$46, U2.P$21; no longer U$1.P$46, U$2.P$21
- net DQD3_P: now also U1.P$45, U2.P$22; no longer U$1.P$45, U$2.P$22
- net DQD4_N: now also U1.P$48, U2.P$16; no longer U$1.P$48, U$2.P$16
- net DQD4_P: now also U1.P$47, U2.P$17; no longer U$1.P$47, U$2.P$17
- net DQD5_N: now also U1.P$50, U2.P$14; no longer U$1.P$50, U$2.P$14
- net DQD5_P: now also U1.P$49, U2.P$15; no longer U$1.P$49, U$2.P$15
- net DQD6_N: now also U1.P$55, U2.P$11; no longer U$1.P$55, U$2.P$11
- net DQD6_P: now also U1.P$54, U2.P$12; no longer U$1.P$54, U$2.P$12
- net DQD7_N: now also U1.P$57, U2.P$9; no longer U$1.P$57, U$2.P$9
- net DQD7_P: now also U1.P$56, U2.P$10; no longer U$1.P$56, U$2.P$10
- net FPGA_CCLK: now also R53.1, R54.2, U13.P$3, U2.P$70; no longer R35.1, R36.2, U$2.P$70, U$7.P$3
- net FPGA_CLK1: now also U2.P$55; no longer U$2.P$55
- net FPGA_CLK2: now also U2.P$56; no longer U$2.P$56
- net FPGA_CSO: now also U2.P$38; no longer U$2.P$38
- net FPGA_CTS: now also U14.4, U2.P$58; no longer IC2.4, U$2.P$58
- net FPGA_DIN: now also U13.P$1, U2.P$65; no longer U$2.P$65, U$7.P$1
- net FPGA_DONE: now also R55.1, U13.P$10, U2.P$71; no longer R38.1, U$2.P$71, U$7.P$10
- net FPGA_DOUT: now also U2.P$74; no longer U$2.P$74
- net FPGA_GPIO1: now also U2.P$47, X3.P$4; no longer U$2.P$47, U$95.P$4
- net FPGA_GPIO2: now also U2.P$48, X3.P$2; no longer U$2.P$48, U$95.P$2
- net FPGA_GPIO3: now also U2.P$57, X3.P$1; no longer U$2.P$57, U$95.P$1
- net FPGA_GPIO4: now also U2.P$62, X3.P$3; no longer U$2.P$62, U$95.P$3
- net FPGA_INITB: now also R59.1, U13.P$8, U2.P$39; no longer R37.1, U$2.P$39, U$7.P$8
- net FPGA_MOSI: now also U2.P$66; no longer U$2.P$66
- net FPGA_PROGRAMB: now also R58.2, R9.1, U2.P$37; no longer R39.2, R7.1, U$2.P$37
- net FPGA_RXD: now also R56.2, U2.P$67; no longer R47.2, U$2.P$67
- net FPGA_SCL: now also R41.1, U10.P$7, U11.P$5, U2.P$43; no longer R50.1, U$2.P$43, U$8.P$7, U$9.P$5
- net FPGA_SDA: now also R44.1, U10.P$6, U11.P$4, U2.P$44; no longer R49.1, U$2.P$44, U$8.P$6, U$9.P$4
- net FPGA_TCK: now also U13.P$6, U2.P$109, X4.6; no longer U$2.P$109, U$7.P$6, X1.6
- net FPGA_TDI: now also U2.P$110, X4.10; no longer U$2.P$110, X1.10
- net FPGA_TDO: now also U13.P$4, U2.P$106; no longer U$2.P$106, U$7.P$4
- net FPGA_TMS: now also U13.P$5, U2.P$107, X4.4; no longer U$2.P$107, U$7.P$5, X1.4
- net FPGA_TXD: now also R57.2, U2.P$64; no longer R48.2, U$2.P$64
- net FTDI_RXD: now also R57.1, U14.2; no longer IC2.2, R48.1
- net FTDI_TXD: now also R56.1, U14.15; no longer IC2.15, R47.1
- net GND: now also C101.P$1, C103.P$1, C105.P$1, C12.2, C13.2, C15.2, C16.2, C17.2, C2.2, C20.2, C22.2, C23.2, C24.2, C25.2, C26.2, C30.2, C33.P$2, C34.P$2, C39.2, C40.2, C47.P$1, C49.P$1, C5.2, C53.P$2, C54.P$2, C55.P$2, C56.P$2, C57.P$2, C58.P$2, C6.P$2, C64.P$1, C65.P$2, C66.P$2, C67.P$2, C68.P$2, C69.P$2, C7.P$2, C70.P$2, C71.P$2, C72.P$2, C73.P$1, C74.P$2, C75.P$2, C76.P$2, C8.2, C82.P$2, C83.2, C84.P$2, C85.2, C86.P$2, C88.2, C9.2, C91.P$2, C93.2, C94.2, C96.P$2, C97.2, L1.P$4, R10.1, R12.2, R14.1, R15.1, R19.1, R2.1, R22.1, R30.1, R31.1, R34.1, R37.1, R39.1, R40.1, R54.1, R7.1, U1.P$1, U1.P$108, U1.P$119, U1.P$12, U1.P$129, U1.P$130, U1.P$131, U1.P$132, U1.P$133, U1.P$134, U1.P$135, U1.P$136, U1.P$137, U1.P$138, U1.P$139, U1.P$140, U1.P$141, U1.P$142, U1.P$143, U1.P$144, U1.P$21, U1.P$24, U1.P$27, U1.P$41, U1.P$42, U1.P$53, U1.P$6, U1.P$64, U1.P$74, U1.P$87, U1.P$9, U1.P$97, U10.P$3, U10.P$4, U10.P$5, U11.P$3, U11.P$6, U12.8, U13.P$11, U14.13, U14.3, U14.TAB, U2.P$108, U2.P$113, U2.P$13, U2.P$130, U2.P$136, U2.P$25, U2.P$3, U2.P$49, U2.P$54, U2.P$60, U2.P$68, U2.P$73, U2.P$77, U2.P$91, U2.P$96, U3.P$11, U3.P$6, U4.2, U4.4, U5.2, U5.4, U6.3, U6.6, U7.P$16, U7.P$18, U7.P$37, U7.P$39, U8.P$1, U8.P$14, U8.P$15, U8.P$17, U8.P$2, U8.P$3, U8.P$4, U8.P$6, U8.P$7, U9.P$2, X1.G@1, X1.G@2, X1.G@3, X1.G@4, X3.P$8, X4.1, X4.11, X4.13, X4.3, X4.5, X4.7, X4.9; no longer C10.P$1, C101.2, C103.2, C105.2, C11.P$2, C12.P$2, C13.P$1, C14.P$2, C15.P$2, C16.P$1, C17.P$2, C20.P$2, C22.P$2, C23.P$2, C24.P$2, C25.P$2, C26.P$2, C27.P$2, C28.P$2, C29.P$2, C30.P$2, C34.2, C39.P$2, C40.P$2, C47.P$2, C49.P$2, C53.2, C55.2, C56.2, C57.2, C58.2, C6.2, C64.P$2, C65.2, C67.2, C68.2, C69.2, C7.2, C70.2, C72.2, C73.2, C74.2, C75.2, C76.2, C77.P$2, C78.P$2, C8.P$2, C83.P$2, C84.2, C85.P$2, C86.2, C9.P$1, C91.2, C93.P$2, C94.P$2, C96.P$1, C97.P$1, IC1.3, IC1.6, IC2.13, IC2.3, IC2.TAB, IC3.8, L2.P$4, R11.1, R16.1, R17.1, R20.1, R23.1, R25.1, R26.1, R29.1, R3.1, R32.2, R33.1, R41.1, R59.1, R62.1, R9.1, U$1.P$1, U$1.P$108, U$1.P$119, U$1.P$12, U$1.P$129, U$1.P$130, U$1.P$131, U$1.P$132, U$1.P$133, U$1.P$134, U$1.P$135, U$1.P$136, U$1.P$137, U$1.P$138, U$1.P$139, U$1.P$140, U$1.P$141, U$1.P$142, U$1.P$143, U$1.P$144, U$1.P$21, U$1.P$24, U$1.P$27, U$1.P$41, U$1.P$42, U$1.P$53, U$1.P$6, U$1.P$64, U$1.P$74, U$1.P$87, U$1.P$9, U$1.P$97, U$10.P$1, U$10.P$14, U$10.P$15, U$10.P$17, U$10.P$2, U$10.P$3, U$10.P$4, U$10.P$6, U$10.P$7, U$11.P$2, U$14.P$11, U$14.P$6, U$2.P$108, U$2.P$113, U$2.P$13, U$2.P$130, U$2.P$136, U$2.P$25, U$2.P$3, U$2.P$49, U$2.P$54, U$2.P$60, U$2.P$68, U$2.P$73, U$2.P$77, U$2.P$91, U$2.P$96, U$4.P$16, U$4.P$18, U$4.P$37, U$4.P$39, U$5.2, U$5.4, U$6.2, U$6.4, U$7.P$11, U$8.P$3, U$8.P$4, U$8.P$5, U$9.P$3, U$9.P$6, U$95.P$8, X1.1, X1.11, X1.13, X1.3, X1.5, X1.7, X1.9, X3.G@1, X3.G@2, X3.G@3, X3.G@4
- net N$1: now also R38.2; no longer R14.2
- net N$10: now also R62.2; no longer R45.2
- net N$11: now also R58.1, U13.P$7; no longer R39.1, U$7.P$7
- net N$12: now also R13.1, R15.2, U3.P$10; no longer R34.1, R41.2, U$14.P$10
- net N$13: now also R63.2; no longer R46.2
- net N$14: now also R29.1, R30.2, U6.5; no longer IC1.5, R22.1, R26.2
- net N$15: now also R42.2, R43.1, U12.1; no longer IC3.1, R54.2, R57.1
- net N$17: now also C9.1, U3.P$8; no longer C105.1, U$14.P$8
- net N$18: now also R50.1, R51.2, R52.1; no longer R60.1, R61.1, R62.2
- net N$19: now also R49.2; no longer R44.2
- net N$2: now also R39.2, U8.P$5; no longer R51.2, U$10.P$5
- net N$20: now also R46.2, R47.1, U12.2; no longer IC3.2, R55.2, R56.1
- net N$21: now also R48.2; no longer R43.2
- net N$22: now also R45.2; no longer R42.2
- net N$24: now also C6.P$1, L1.P$3, L2.P$1; no longer C20.P$1, L2.P$3, L5.P$1
- net N$3: now also R60.2, U14.6; no longer IC2.6, R52.2
- net N$34: now also L1.P$1; no longer L2.P$1
- net N$35: now also L1.P$2; no longer L2.P$2
- net N$4: now also R60.1; no longer R52.1
- net N$5: now also R61.1; no longer R53.1
- net N$6: now also R13.2; no longer R34.2
- net N$7: now also R61.2, U14.7; no longer IC2.7, R53.2
- net PGOOD: now also R21.1, U2.P$35, U7.P$15; no longer R12.1, U$2.P$35, U$4.P$15
- net PROM_TDO: now also U13.P$17, X4.8; no longer U$7.P$17, X1.8
- net PWR_ENABLE: now also U3.P$3, U7.P$13, U7.P$33; no longer U$14.P$3, U$4.P$13, U$4.P$33
- net PWR_INT: now also R23.1, U2.P$59, U3.P$1; no longer R64.1, U$14.P$1, U$2.P$59
- net PWR_KILL: now also R25.1, U2.P$61, U3.P$9; no longer R63.1, U$14.P$9, U$2.P$61
- net S1EN: now also C23.1, R27.2, R28.2, U7.P$38; no longer C7.1, R13.2, R16.2, U$4.P$38
- net S1FB: now also C29.2, R35.1, R37.2, U7.P$1; no longer C5.2, R15.1, R17.2, U$4.P$1
- net S1SW: now also L8.P$1, U7.P$3, U7.P$4; no longer L3.P$1, U$4.P$3, U$4.P$4
- net S3EN: now also C5.1, R11.2, R12.1, U7.P$14; no longer C75.1, R30.2, R32.1, U$4.P$14
- net S3FB: now also C11.2, R17.1, R19.2, U7.P$7; no longer C71.2, R31.1, R33.2, U$4.P$7
- net S3SW: now also L4.P$1, U7.P$9; no longer L10.P$1, U$4.P$9
- net S4FB: now also C27.2, R32.1, R34.2, U7.P$12; no longer C33.2, R19.1, R20.2, U$4.P$12
- net S4SW: now also L6.P$1, U7.P$10; no longer L7.P$1, U$4.P$10
- net S5FB: now also C14.2, R20.1, R22.2, U7.P$20; no longer C54.2, R21.1, R24.2, U$4.P$20
- net S5SW: now also L5.P$1, U7.P$22, U7.P$23; no longer L8.P$1, U$4.P$22, U$4.P$23
- net S7FB: now also C28.2, R33.1, R36.2, U7.P$26; no longer C2.2, R10.1, R11.2, U$4.P$26
- net S7SW: now also L7.P$1, U7.P$28; no longer L1.P$1, U$4.P$28
- net S8FB: now also C10.2, R16.1, R18.2, U7.P$31; no longer C66.2, R27.1, R29.2, U$4.P$31
- net S8SW: now also L3.P$1, U7.P$29; no longer L9.P$1, U$4.P$29
- net SIGNAL_IN: now also U8.P$16, X1.1; no longer U$10.P$16, X2.1
- net S_MODE: now also R24.2, R26.2, U7.P$34; no longer R18.2, R40.2, U$4.P$34
- net S_TEMP: now also U7.P$36, X3.P$6; no longer U$4.P$36, U$95.P$6
- net TRIGGER: now also R40.2, U12.3, X2.1; no longer IC3.3, R59.2, X3.1
- net TRIG_REF: now also U11.P$1, U12.4; no longer IC3.4, U$9.P$1
- net TRIG_RESET_HIGH: now also R46.1, U2.P$45; no longer R55.1, U$2.P$45
- net TRIG_RESET_LOW: now also R42.1, U2.P$46; no longer R54.1, U$2.P$46
- net VIN: now also C2.1, C20.1, C22.1, C3.1, C7.P$1, C8.1, L2.P$2, R26.1, U3.P$4, U3.P$7, U7.P$11, U7.P$17, U7.P$2, U7.P$21, U7.P$24, U7.P$25, U7.P$27, U7.P$30, U7.P$35, U7.P$5, U7.P$6, U7.P$8; no longer C30.P$1, C32.1, C53.1, C58.1, C65.1, C70.1, L5.P$2, R40.1, U$14.P$4, U$14.P$7, U$4.P$11, U$4.P$17, U$4.P$2, U$4.P$21, U$4.P$24, U$4.P$25, U$4.P$27, U$4.P$30, U$4.P$35, U$4.P$5, U$4.P$6, U$4.P$8
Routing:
- net FPGA_TRIG_P: track 0.00 -> 94.5 mm, vias 0 -> 2
- net FPGA_TRIG_N: track 0.00 -> 92.9 mm, vias 0 -> 2
- net FPGA_TRIG+: track 84.3 -> 0.00 mm, vias 2 -> 0
- net FPGA_TRIG-: track 84.2 -> 0.00 mm, vias 2 -> 0
- net TRIG_RESET_LOW: track 81.9 -> 97.4 mm
- net TRIG_RESET_HIGH: track 78.2 -> 93.3 mm
- net ADC_PDQ: track 53.8 -> 64.3 mm
- net ADC_PD: track 73.1 -> 83.2 mm
- net ADC_CAL: track 66.7 -> 76.4 mm
- net FPGA_SDA: track 99.5 -> 108.7 mm
- net FPGA_SCL: track 104.3 -> 113.4 mm
- net GND: track 233.0 -> 233.8 mm
- net 5VUSB: track 16.0 -> 16.7 mm
- net N$20: track 13.2 -> 12.5 mm
- net N$15: track 11.1 -> 10.5 mm
- removed copper zone on layer 1, net 5VUSB
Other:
- board text added: "Manufacturer Notes: 1. All copper thickness is 1oz 2. LVDS lines are 5mil width with 5mil spacing and should have a 100 Ohms+/- 10% differential impedance."
- board text removed: "Manufacturer Notes: 1. All copper thickness is 1oz 2. LVDS lines are 5mil width with 5mil spacing and should have a 100 Ohms+/- 10% differential impedance. 3. Layer height is betwen 7 and 8 mils."
